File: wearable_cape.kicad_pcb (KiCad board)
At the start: 2 copper layers, 72.6 x 54.6 mm, 66 parts, among them J1 J1 0 5, J2 J2 2 3, J3 J3 1 4, P1 BELA_AINS, P2 SERIAL_BREAKOUT, P3 CONN_01X02_BATTERY, P4 BELA_AOUTS, P5 PWR_OUT_AMPS, P6 STATUS_BREAKOUT, P7 A_IN_BREAKOUT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

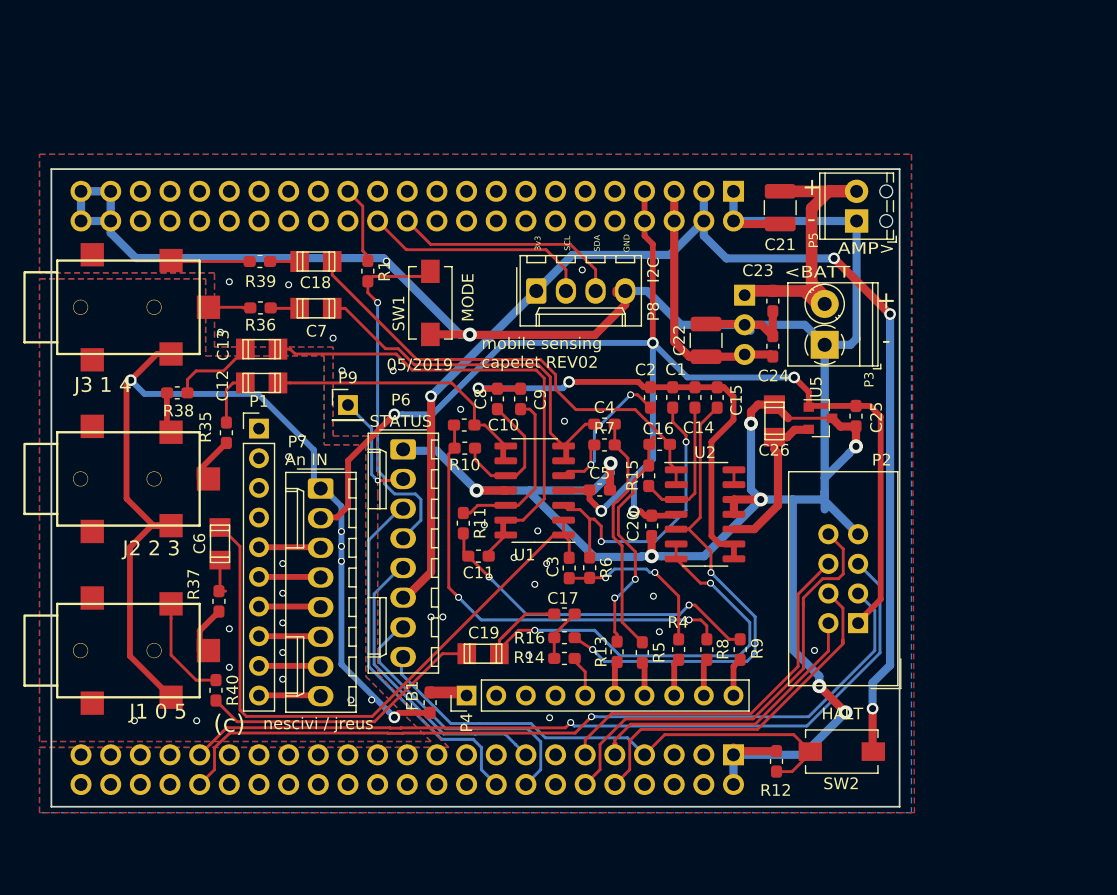
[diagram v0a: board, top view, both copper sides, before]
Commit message: updates - wiring mistake!
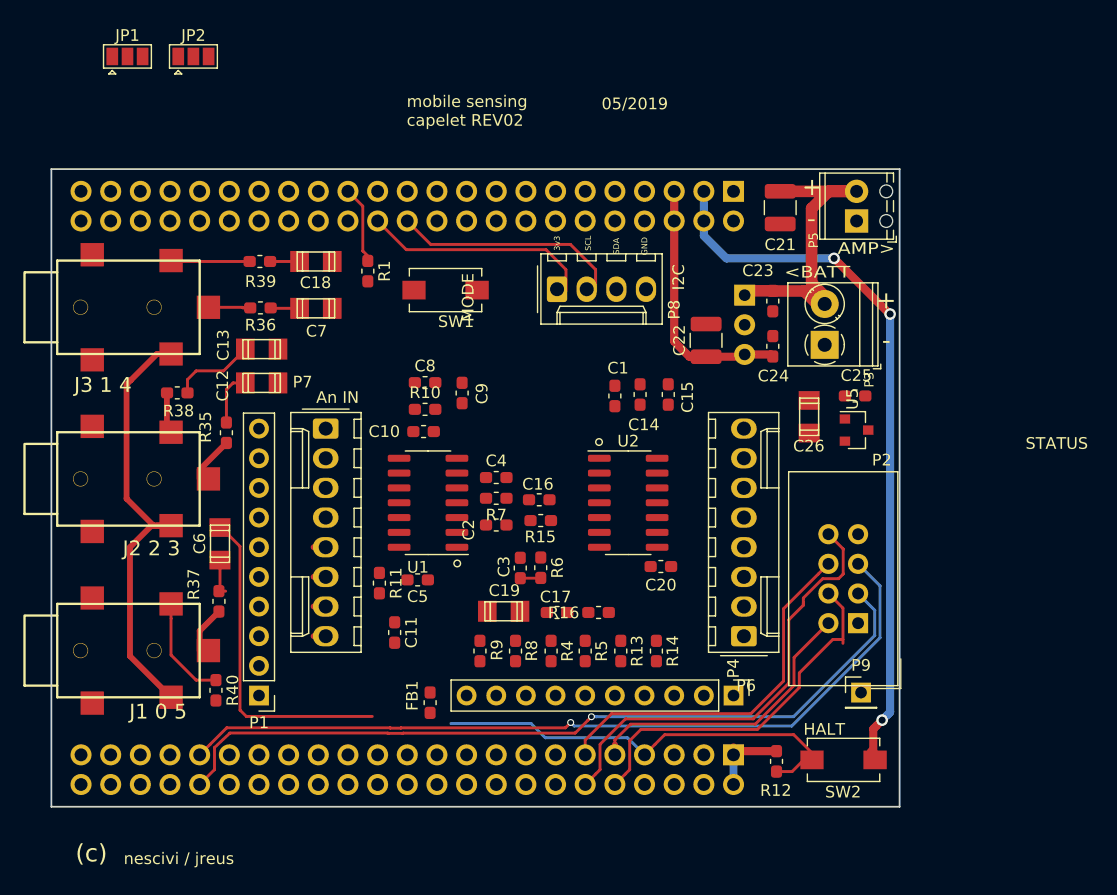
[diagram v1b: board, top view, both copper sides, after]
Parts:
- added JP1: serial power select, jcr-device:SolderJumper-3_P1.3mm_Open_Pad1.0x1.5mm, F.Cu at (38.3, 8.77)
- added JP2: analog power select, jcr-device:SolderJumper-3_P1.3mm_Open_Pad1.0x1.5mm, F.Cu at (43.9, 8.77)
- moved P9 50.4 mm to (101.1, 63.2)
- moved P6 33.3 mm to (91.1, 58.4), turned to 90 degrees
- moved P1 22.9 mm to (49.5, 63.5), turned to 180 degrees
- moved P4 22.9 mm to (90.2, 63.5), turned to 270 degrees
- moved R9 22.3 mm to (68.5, 59.7)
- moved C5 17.4 mm to (63.1, 53.6), turned to 180 degrees
- moved C2 17.1 mm to (69.8, 48.9), turned to 180 degrees
- moved R8 16.4 mm to (71.5, 59.7)
- moved C16 11.4 mm to (73.5, 46.7)
- moved R4 10.9 mm to (74.5, 59.7)
- moved C4 10.3 mm to (69.8, 44.8)
- moved R7 10.3 mm to (69.8, 46.6), turned to 180 degrees
- moved R15 10.0 mm to (73.7, 48.5), turned to 180 degrees
- moved C11 9.71 mm to (61.2, 58.1), turned to 270 degrees
- moved U1 9.19 mm to (64.0, 47.0)
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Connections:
- P2 pad 1: SYS_5V -> Net-(JP1-Pad2)
- P6 pad 2: /STATUS_LED -> /~SW_HALT
- P6 pad 3: /D11 -> SYS_3.3V
- P6 pad 4: /~SW_HALT -> /D0
- P6 pad 5: /D8 -> /D11
- P6 pad 6: SYS_3.3V -> /D8
- P6 pad 8: /D0 -> /STATUS_LED
- P7 pad 2: SYS_5V -> Net-(JP2-Pad2)
- P7 pad 3: /BELA_IN5 -> /BELA_IN0
- P7 pad 4: /BELA_IN4 -> /BELA_IN1
- P7 pad 5: /BELA_IN3 -> /BELA_IN2
- P7 pad 6: /BELA_IN2 -> /BELA_IN3
- P7 pad 7: /BELA_IN1 -> /BELA_IN4
- P7 pad 8: /BELA_IN0 -> /BELA_IN5
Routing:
- net GND: track 265.9 -> 6.99 mm, vias 31 -> 0
- net SYS_5V: track 124.3 -> 0.00 mm, vias 5 -> 0
- net SYS_3.3V: track 109.2 -> 60.8 mm, vias 4 -> 3
- net GNDA: track 87.5 -> 39.3 mm, vias 18 -> 0
- net Net-(C17-Pad1): track 43.2 -> 0.00 mm, vias 2 -> 0
- net REF_1.8V: track 42.4 -> 0.00 mm, vias 2 -> 0
- net Net-(C15-Pad1): track 41.9 -> 0.00 mm, vias 2 -> 0
- net Net-(C11-Pad1): track 41.9 -> 0.00 mm
- net Net-(C16-Pad1): track 40.6 -> 0.00 mm
- net Net-(C10-Pad2): track 38.8 -> 0.00 mm, vias 2 -> 0
- net Net-(C4-Pad1): track 32.7 -> 0.00 mm
- net /~SW_HALT: track 31.5 -> 0.00 mm, vias 1 -> 0
- net /D11: track 30.9 -> 0.00 mm
- net Net-(C11-Pad2): track 29.1 -> 0.00 mm, vias 2 -> 0
- net Net-(C3-Pad1): track 54.2 -> 28.0 mm
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- removed copper zone on B.Cu, net GND
- removed copper zone on F.Cu, net GND
- removed copper zone on B.Cu, net GNDA
- removed copper zone on F.Cu, net GNDA
